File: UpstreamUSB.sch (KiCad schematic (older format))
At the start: 8 parts, among them J1 USB_B, U4 TPS76333

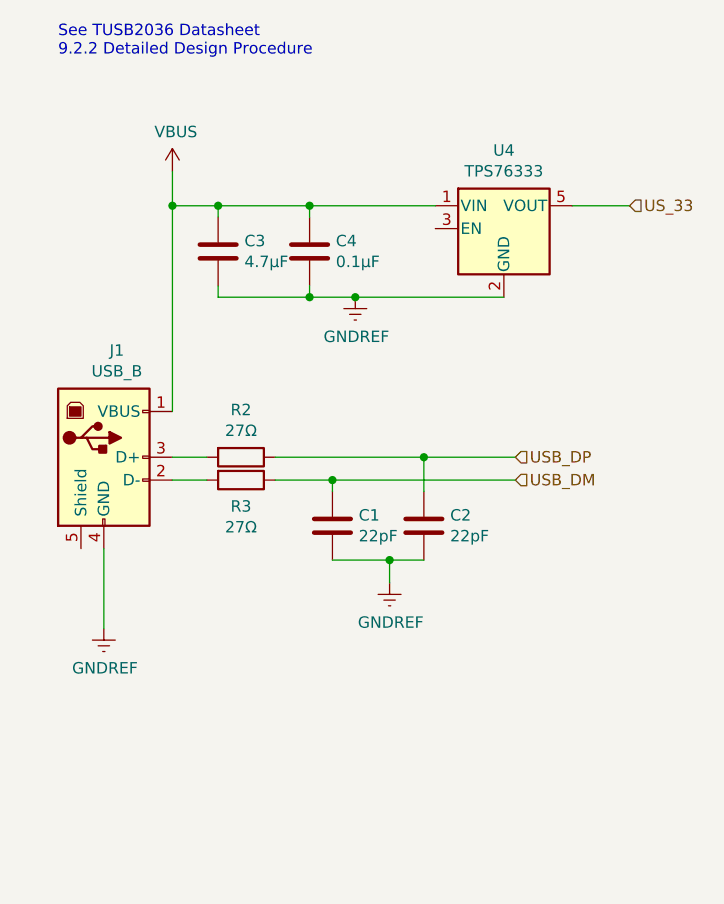
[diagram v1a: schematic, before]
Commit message: Add ID markings on schema and pcb
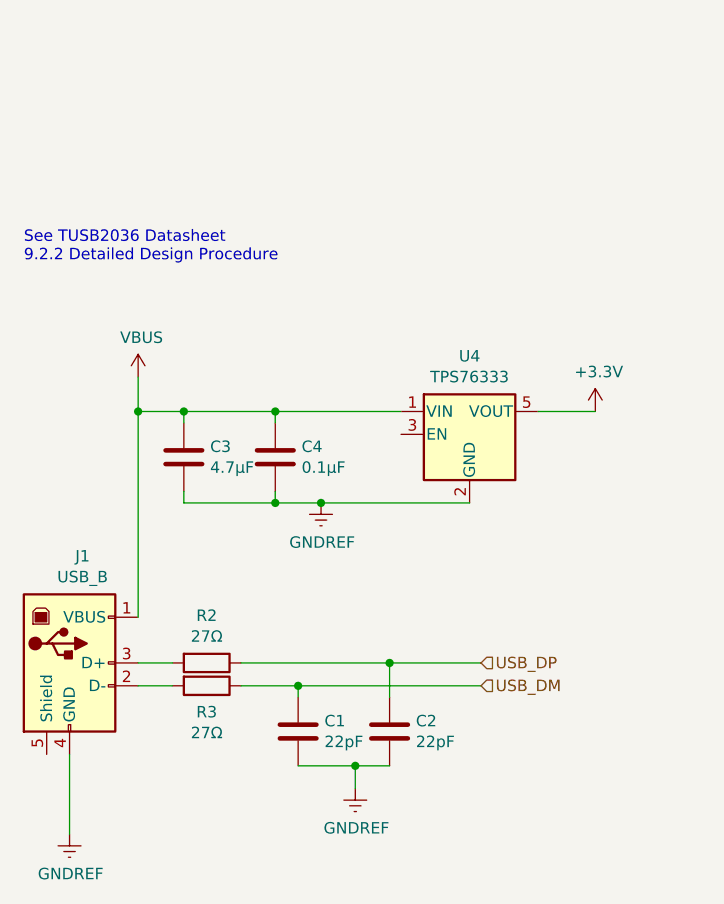
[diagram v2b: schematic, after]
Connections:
- net US_33 renamed +3V3
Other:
- moved on the sheet: C1, C2, C3, C4, J1, R2, R3, U4

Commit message: First pass at routing PCB
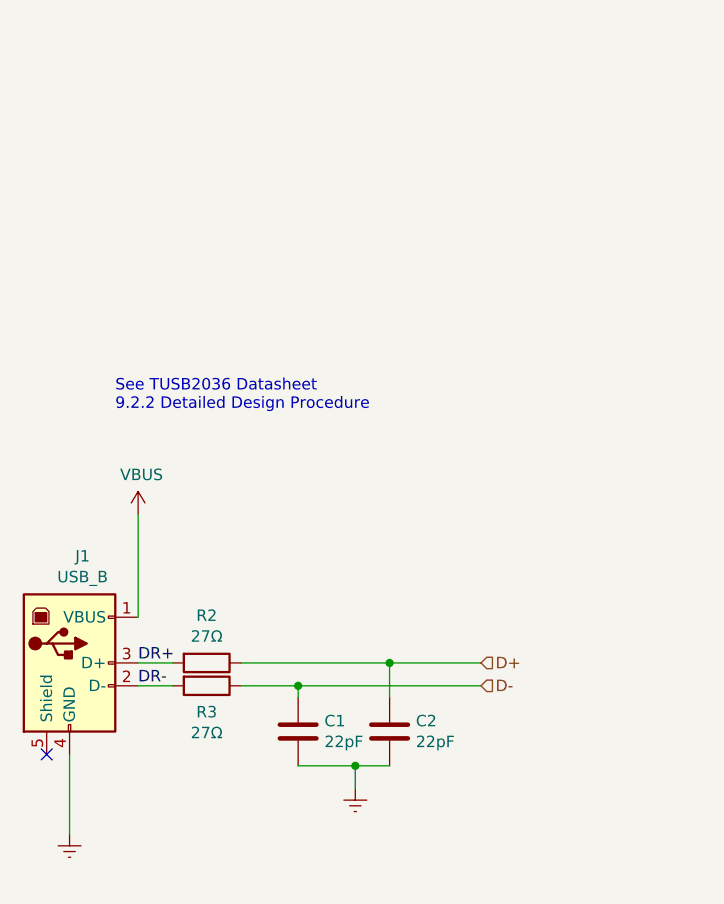
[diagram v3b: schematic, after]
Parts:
- removed C3: 4.7μF, Capacitor_SMD:C_1210_3225Metric, symbol Device:C
- removed C4: 0.1μF, Capacitor_SMD:C_1210_3225Metric, symbol Device:C
- removed U4: TPS76333, Package_TO_SOT_SMD:SOT-23-5, symbol Regulator_Linear:TPS76333
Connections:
- net DR+: now reaches J1.3 (D+), R2.2
- net DR-: now reaches J1.2 (D-), R3.2
- net USB_DM renamed D-
- net USB_DP renamed D+
- no-connect marks 0 -> 1
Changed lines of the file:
@@
 Rev "0.1"
 Comp "Chris Keller K0SWE"
-Comment1 ""
+Comment1 "Licensed under Apache-2.0"
 Comment2 ""
 Comment3 ""
@@
 P 5600 4600
 F 0 "#PWR0125" H 5600 4350 50  0001 C CNN
-F 1 "GNDREF" H 5605 4427 50  0000 C CNN
+F 1 "GNDREF" H 5605 4427 50  0001 C CNN
 F 2 "" H 5600 4600 50  0001 C CNN
 F 3 "" H 5600 4600 50  0001 C CNN
@@
 P 4350 4800
 F 0 "#PWR0126" H 4350 4550 50  0001 C CNN
-F 1 "GNDREF" H 4355 4627 50  0000 C CNN
+F 1 "GNDREF" H 4355 4627 50  0001 C CNN
 F 2 "" H 4350 4800 50  0001 C CNN
 F 3 "" H 4350 4800 50  0001 C CNN
@@
 $EndComp
 $Comp
-L Regulator_Linear:TPS76333 U4
-U 1 1 604D068E
-P 6100 3050
-F 0 "U4" H 6100 3392 50  0000 C CNN
-F 1 "TPS76333" H 6100 3301 50  0000 C CNN
-F 2 "Package_TO_SOT_SMD:SOT-23-5" H 6100 3375 50  0001 C CIN
-F 3 "http://www.ti.com/lit/ds/symlink/tps763.pdf" H 6100 3050 50  0001 C CNN
-F 4 "Voltage Regulator" H 6100 3492 50  0001 C CNN "Description"
-F 5 "TI" H 6100 3492 50  0001 C CNN "Manufacturer_Name"
-F 6 "TPS76333" H 6100 3492 50  0001 C CNN "Manufacturer_Part_Number"
-F 7 "0.97" H 6100 3492 50  0001 C CNN "Price"
-F 8 "595-TPS76333DBVTG4" H 6100 3492 50  0001 C CNN "Vendor Part Number"
-F 9 "Mouser" H 6100 3492 50  0001 C CNN "Vendor"
-	1    6100 3050
-	1    0    0    -1
-$EndComp
-$Comp
-L Device:C C3
-U 1 1 604D10A1
-P 4850 3150
-F 0 "C3" H 4965 3196 50  0000 L CNN
-F 1 "4.7μF" H 4965 3105 50  0000 L CNN
-F 2 "Capacitor_SMD:C_1210_3225Metric" H 4888 3000 50  0001 C CNN
-F 3 "https://www.mouser.com/datasheet/2/210/WTC_MLCC_General_Purpose-1534899.pdf" H 4850 3150 50  0001 C CNN
-F 4 "Walsin" H 4965 3296 50  0001 C CNN "Manufacturer_Name"
-F 5 "1210F475Z500CT" H 4965 3296 50  0001 C CNN "Manufacturer_Part_Number"
-F 6 "0.62" H 4965 3296 50  0001 C CNN "Price"
-F 7 "791-1210F475Z500CT" H 4965 3296 50  0001 C CNN "Vendor Part Number"
-F 8 "Mouser" H 4965 3296 50  0001 C CNN "Vendor"
-	1    4850 3150
-	1    0    0    -1
-$EndComp
-$Comp
-L Device:C C4
-U 1 1 604D3F79
-P 5250 3150
-F 0 "C4" H 5365 3196 50  0000 L CNN
-F 1 "0.1μF" H 5365 3105 50  0000 L CNN
-F 2 "Capacitor_SMD:C_1210_3225Metric" H 5288 3000 50  0001 C CNN
-F 3 "https://www.mouser.com/datasheet/2/212/KEM_C1007_X8R_ULTRA_150C_SMD-1102703.pdf" H 5250 3150 50  0001 C CNN
-F 4 "KEMET" H 5365 3296 50  0001 C CNN "Manufacturer_Name"
-F 5 "C1210C104K5HACAUTO" H 5365 3296 50  0001 C CNN "Manufacturer_Part_Number"
-F 6 "0.5" H 5365 3296 50  0001 C CNN "Price"
-F 7 "80-C1210C104K5HAUTO" H 5365 3296 50  0001 C CNN "Vendor Part Number"
-F 8 "Mouser" H 5365 3296 50  0001 C CNN "Vendor"
-	1    5250 3150
-	1    0    0    -1
-$EndComp
-$Comp
-L power:GNDREF #PWR0127
-U 1 1 604D4746
-P 5450 3350
-F 0 "#PWR0127" H 5450 3100 50  0001 C CNN
-F 1 "GNDREF" H 5455 3177 50  0000 C CNN
-F 2 "" H 5450 3350 50  0001 C CNN
-F 3 "" H 5450 3350 50  0001 C CNN
-	1    5450 3350
-	1    0    0    -1
-$EndComp
-$Comp
 L power:VBUS #PWR0128
 U 1 1 604FCE55
-P 4650 2800
-F 0 "#PWR0128" H 4650 2650 50  0001 C CNN
-F 1 "VBUS" H 4665 2973 50  0000 C CNN
-F 2 "" H 4650 2800 50  0001 C CNN
-F 3 "" H 4650 2800 50  0001 C CNN
-	1    4650 2800
+P 4650 3400
+F 0 "#PWR0128" H 4650 3250 50  0001 C CNN
+F 1 "VBUS" H 4665 3573 50  0000 C CNN
+F 2 "" H 4650 3400 50  0001 C CNN
+F 3 "" H 4650 3400 50  0001 C CNN
+	1    4650 3400
 	1    0    0    -1
 $EndComp
 Text HLabel 6150 4050 2    50   Input ~ 0
-USB_DP
+D+
 Text HLabel 6150 4150 2    50   Input ~ 0
-USB_DM
-Text Notes 4150 2300 0    50   ~ 0
+D-
+Text Notes 4550 2950 0    50   ~ 0
 See TUSB2036 Datasheet\n9.2.2 Detailed Design Procedure
 Wire Wire Line
@@
 	4350 4450 4350 4800
 Wire Wire Line
-	4650 3850 4650 2950
-Wire Wire Line
-	5450 3350 5250 3350
-Wire Wire Line
-	6100 3350 5450 3350
-Wire Wire Line
-	5250 3300 5250 3350
-Wire Wire Line
-	5250 3000 5250 2950
-Wire Wire Line
-	5250 2950 5800 2950
-Wire Wire Line
-	4650 2950 4850 2950
-Wire Wire Line
-	4850 3000 4850 2950
-Wire Wire Line
-	4850 2950 5250 2950
-Wire Wire Line
-	4850 3300 4850 3350
-Wire Wire Line
-	4850 3350 5250 3350
-Wire Wire Line
 	5100 4150 5350 4150
 Wire Wire Line
@@
 Wire Wire Line
 	5350 4500 5600 4500
-Wire Wire Line
-	6400 2950 6650 2950
-Wire Wire Line
-	4650 2800 4650 2950
 Connection ~ 5600 4500
 Connection ~ 5750 4050
-Connection ~ 5250 3350
-Connection ~ 5450 3350
-Connection ~ 5250 2950
-Connection ~ 4850 2950
 Connection ~ 5350 4150
-Connection ~ 4650 2950
-$Comp
-L power:+3.3V #PWR?
-U 1 1 6053FA2A
-P 6650 2950
-F 0 "#PWR?" H 6650 2800 50  0001 C CNN
-F 1 "+3.3V" H 6665 3123 50  0000 C CNN
-F 2 "" H 6650 2950 50  0001 C CNN
-F 3 "" H 6650 2950 50  0001 C CNN
-	1    6650 2950
-	1    0    0    -1
-$EndComp
+Wire Wire Line
+	4650 3400 4650 3850
+NoConn ~ 4250 4450
+Text Label 4650 4050 0    50   ~ 0
+DR+
+Text Label 4650 4150 0    50   ~ 0
+DR-
 $EndSCHEMATC

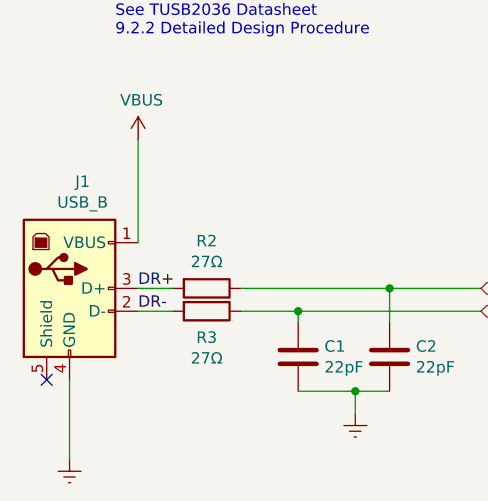
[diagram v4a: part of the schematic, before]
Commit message: Adjust USB connectors to start case CAD
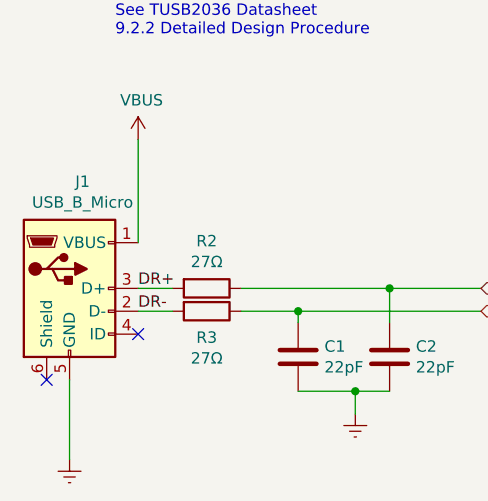
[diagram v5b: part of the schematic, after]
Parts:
- removed J1: USB_B, Connector_USB:USB_Micro-B_Molex_47346-0001, symbol Connector:USB_B
- added J1: USB_B_Micro, Connector_USB:USB_Micro-B_Molex_47346-0001, symbol Connector:USB_B_Micro
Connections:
- net DR+: now also J1.3 (D+)
- net DR-: now also J1.2 (D-)
- net GNDREF: now also J1.5 (GND)
- net VBUS: now also J1.1 (VBUS)
- no-connect marks 1 -> 2
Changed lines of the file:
@@
 $EndDescr
-$Comp
-L Connector:USB_B J?
-U 1 1 60570101
-P 4350 4050
-AR Path="/60570101" Ref="J?"  Part="1"
-AR Path="/6057976E/60570101" Ref="J1"  Part="1"
-F 0 "J1" H 4407 4517 50  0000 C CNN
-F 1 "USB_B" H 4407 4426 50  0000 C CNN
-F 2 "Connector_USB:USB_Micro-B_Molex_47346-0001" H 4500 4000 50  0001 C CNN
-F 3 "https://www.mouser.com/datasheet/2/276/0473460001_IO_CONNECTORS-229243.pdf" H 4500 4000 50  0001 C CNN
-F 4 "Upstream USB socket" H 4407 4617 50  0001 C CNN "Description"
-F 5 "Molex" H 4407 4617 50  0001 C CNN "Manufacturer_Name"
-F 6 "47346-0001" H 4407 4617 50  0001 C CNN "Manufacturer_Part_Number"
-F 7 "0.95" H 4407 4617 50  0001 C CNN "Price"
-F 8 "538-47346-0001" H 4407 4617 50  0001 C CNN "Vendor Part Number"
-F 9 "Mouser" H 4407 4617 50  0001 C CNN "Vendor"
-	1    4350 4050
-	1    0    0    -1
-$EndComp
 $Comp
 L Device:R R2
@@
 Connection ~ 5350 4150
 NoConn ~ 4250 4450
+$Comp
+L Connector:USB_B_Micro J1
+U 1 1 60501F1A
+P 4350 4050
+F 0 "J1" H 4407 4517 50  0000 C CNN
+F 1 "USB_B_Micro" H 4407 4426 50  0000 C CNN
+F 2 "Connector_USB:USB_Micro-B_Molex_47346-0001" H 4500 4000 50  0001 C CNN
+F 3 "https://www.mouser.com/datasheet/2/276/0473460001_IO_CONNECTORS-229243.pdf" H 4500 4000 50  0001 C CNN
+	1    4350 4050
+	1    0    0    -1
+$EndComp
+NoConn ~ 4650 4250
 $EndSCHEMATC
